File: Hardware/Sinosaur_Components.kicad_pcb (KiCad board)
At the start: 4 copper layers, 60 x 100 mm, 82 parts, among them J1 Conn_01x12_Male, J2 Conn_01x12_Male, J3 Conn_01x16_Male, J4 Conn_01x16_Male, J5 SWD_Header, J6 Eurorack_16_pin_power, J7 UART_Test_Pins, J8 USB_B_Micro, Q1 MMBT3904, Q2 MMBT3904, U1 STM32G473V, U2 STF202-22T1G, U3 TL074, U4 TL074, U5 LT1117-3.3, Y1 8MHz 20pF

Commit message: Updated file names
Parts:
- moved TP3 55.7 mm to (114.8, 62.2)
- moved TP1 29.1 mm to (143.3, 68.6)
- moved C9 0.50 mm to (117.0, 106.0)
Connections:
- J1 pad 10: unconnected-(J1-Pin_10-Pad10) -> GND
- J2 pad 3: +3.3V -> unconnected-(J2-Pin_3-Pad3)
- J3 pad 12: unconnected-(J3-Pin_12-Pad12) -> /Sine2_Rate
- J3 pad 13: unconnected-(J3-Pin_13-Pad13) -> GND
- J3 pad 14: unconnected-(J3-Pin_14-Pad14) -> +3.3V
- J3 pad 6: /Sine3_Ramp_Lvl_LED -> GND
- J3 pad 7: /Sine1_Swell_Lvl_LED -> /Sine3_Ramp_Lvl_LED
- J3 pad 8: /Sine2_Swell_Lvl_LED -> /Sine1_Swell_Lvl_LED
- J3 pad 9: unconnected-(J3-Pin_9-Pad9) -> /Sine2_Swell_Lvl_LED
- J4 pad 10: /Sine1_Rate_Btn -> /Sine2_Rate_Btn
- J4 pad 11: /Sine3_Lvl_Btn -> /Sine1_Rate_Btn
- J4 pad 12: /Sine2_Lvl_Btn -> /Sine3_Lvl_Btn
- J4 pad 13: /Sine1_Lvl_Btn -> /Sine2_Lvl_Btn
- J4 pad 14: /Gate_In -> /Sine1_Lvl_Btn
- J4 pad 15: /Clock_In -> /Gate_In
- J4 pad 16: GND -> /Clock_In
- J4 pad 8: /Sine3_Rate_Btn -> GND
- J4 pad 9: /Sine2_Rate_Btn -> /Sine3_Rate_Btn
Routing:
- net +3.3V: track 35.6 -> 199.4 mm, vias 0 -> 8
- net /Sine2_Rate: track 0.00 -> 48.6 mm, vias 0 -> 1
- net +3.3VA: track 17.4 -> 53.9 mm, vias 2 -> 3
- net -12V: track 66.6 -> 92.6 mm
- net /Swell_DAC: track 34.5 -> 41.2 mm
- net /Gate_Scaled: track 41.5 -> 44.1 mm
- net /Sine1_Swell_Lvl_LED: track 15.6 -> 18.2 mm
- net /Sine2_Swell_Lvl_LED: track 16.6 -> 19.1 mm
- net /Sine3_Ramp_Lvl_LED: track 14.9 -> 17.4 mm
- net /Sine1_Rate: track 44.6 -> 46.5 mm
- net +12V: track 59.6 -> 61.5 mm
- net /TIM2_CH2: track 24.1 -> 25.3 mm
- net /Sine2_Rate_Btn: track 42.0 -> 43.1 mm
- net /Sine1_Lvl_Btn: track 49.4 -> 50.5 mm
- net /Sine3_Rate_Btn: track 40.2 -> 41.2 mm
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
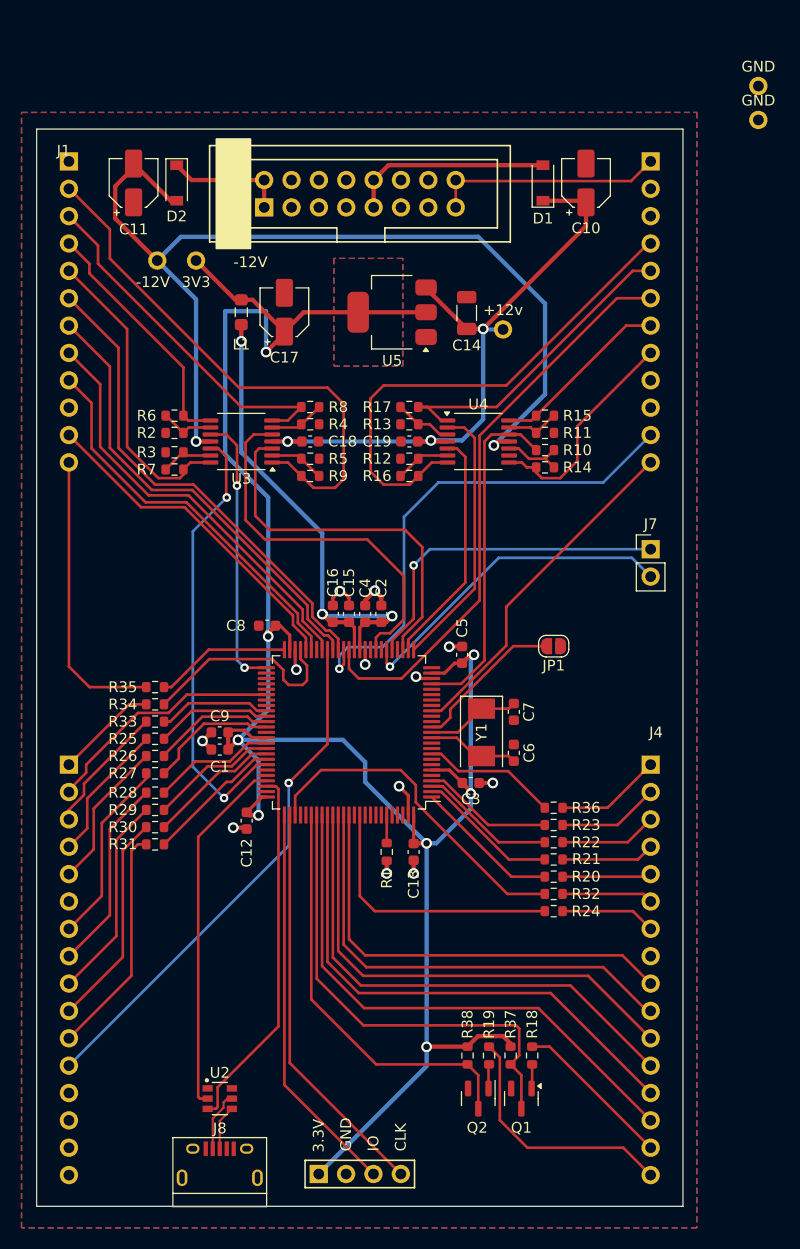
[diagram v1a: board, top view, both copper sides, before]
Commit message: Control PCB wiring
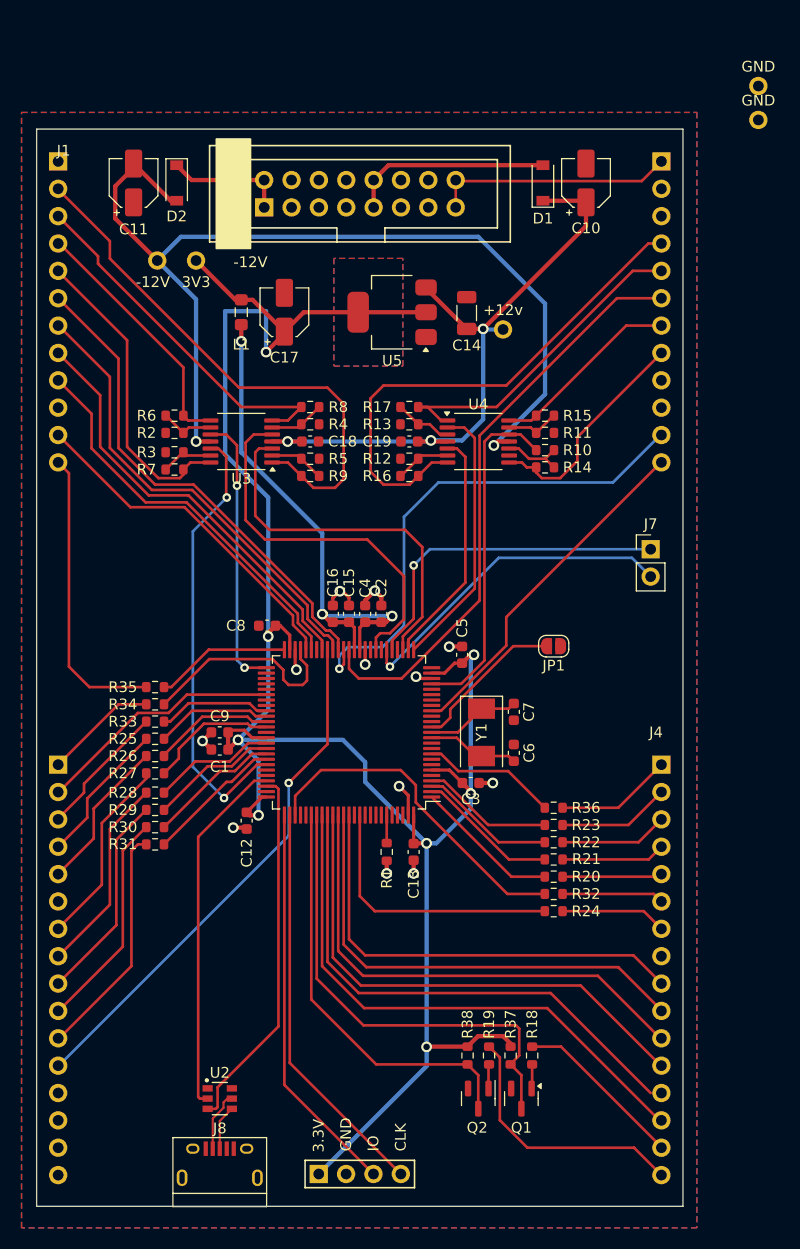
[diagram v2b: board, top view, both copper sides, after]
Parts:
- R25, R26, R27, R28, R29, R30, R31, R32, R33, R34, R35, R36: value 560 -> 1k
- moved J1 1.00 mm to (102.0, 53.0)
- moved J2 1.00 mm to (158.0, 53.0)
- moved J3 1.00 mm to (102.0, 109.0)
- moved J4 1.00 mm to (158.0, 109.0)
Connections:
- J1 pad 8: /Sine3_Rate -> /Swell_Level
- J2 pad 12: /Swell_Level -> /Sine3_Rate
- J2 pad 3: unconnected-(J2-Pin_3-Pad3) -> GND
- J3 pad 15: unconnected-(J3-Pin_15-Pad15) -> GND
- U1 pad 17: /Swell_Level -> /Sine3_Rate
- U1 pad 43: /Sine3_Rate -> /Swell_Level
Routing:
- net /Swell_Level: track 32.0 -> 39.9 mm
- net /Sine3_Rate: track 39.4 -> 32.4 mm
- net /Sine2_Rate_Btn: track 43.1 -> 44.1 mm
- net /Gate_In: track 14.9 -> 15.9 mm
- net /Sine3_Rate_Btn: track 41.2 -> 42.2 mm
- net /Sine3_Level: track 53.7 -> 54.7 mm
- net /Sine1_Rate_Btn: track 45.0 -> 46.0 mm
- net /Swell_LED: track 8.66 -> 9.66 mm
- net /Sine3_Swell_Rate_LED: track 9.83 -> 10.8 mm
- net /Sine3_Out: track 30.0 -> 31.0 mm
- net /Sine3_Lvl_Btn: track 46.9 -> 47.9 mm
- net /Sine3_LED: track 8.85 -> 9.85 mm
- net /Sine2_Ramp_Rate_LED: track 8.46 -> 9.46 mm
- net /Sine2_Out: track 47.2 -> 48.2 mm
- net /Sine2_LED: track 9.44 -> 10.4 mm
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
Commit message: Updates to LEDs
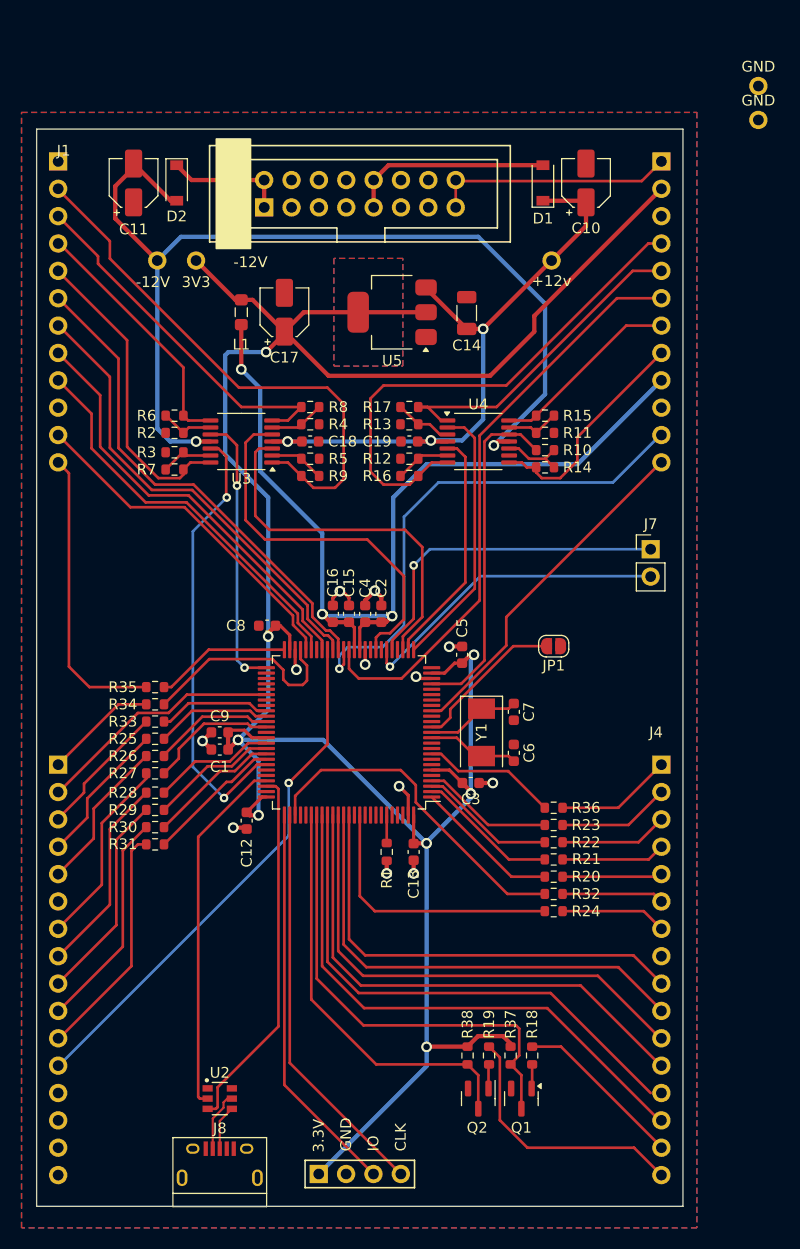
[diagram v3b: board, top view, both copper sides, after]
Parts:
- moved TP1 7.82 mm to (147.8, 62.2)
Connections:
- J2 pad 2: GND -> +3.3V
- J3 pad 14: +3.3V -> GND
- J3 pad 16: unconnected-(J3-Pin_16-Pad16) -> GND
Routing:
- net +3.3VA: track 53.9 -> 94.4 mm
- net +3.3V: track 199.4 -> 234.8 mm
- net +12V: track 61.5 -> 59.7 mm
- net /USART1_RX: track 30.8 -> 29.4 mm
- net -12V: track 92.6 -> 94.0 mm

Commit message: Gerber production
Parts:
- added TP6: TestPoint, Custom_Footprints:1mm_Test_Point, F.Cu at (106.1, 93.8)
- U3, U4: footprint Package_SO:TSSOP-14_4.4x5mm_P0.65mm -> Package_SO:SOIC-14_3.9x8.7mm_P1.27mm
- moved TP5 100.3 mm to (143.0, 146.5)
- moved TP4 54.5 mm to (157.0, 99.6)
- moved TP3 35.6 mm to (150.4, 62.1)
- moved TP1 1.20 mm to (146.6, 62.1)
- moved R10 0.80 mm to (147.2, 80.6), turned to 0 degrees
- moved R11 0.80 mm to (147.2, 77.4)
- moved R14 0.80 mm to (147.2, 82.2), turned to 180 degrees
- moved R15 0.80 mm to (147.2, 75.8)
- moved R2 0.80 mm to (112.8, 77.4)
- moved R6 0.80 mm to (112.8, 75.8)
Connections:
- R10 pad 1: Net-(U4C-+) -> Net-(U4C--)
- R13 pad 2: Net-(U4A-+) -> Net-(U4A--)
- R14 pad 2: Net-(U4C-+) -> Net-(U4C--)
- R17 pad 2: Net-(U4A-+) -> Net-(U4A--)
- U1 pad 10: unconnected-(U1-PF9-Pad10) -> /Sine3_Swell_Rate
- U1 pad 9: /Sine3_Swell_Rate -> unconnected-(U1-PC15-Pad9)
- U4 pad 10: Net-(U4C-+) -> GND
- U4 pad 2: /Sine3_DAC -> Net-(U4A--)
- U4 pad 3: Net-(U4A-+) -> /Sine3_DAC
- U4 pad 9: GND -> Net-(U4C--)
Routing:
- net GND: track 23.3 -> 36.3 mm, vias 12 -> 75
- net +3.3V: track 234.8 -> 228.1 mm, vias 8 -> 30
- net Net-(U4C-+): track 6.02 -> 0.00 mm
- net Net-(U4A--): track 0.00 -> 5.80 mm
- net Net-(U4A-+): track 5.42 -> 0.00 mm
- net Net-(U4C--): track 0.00 -> 4.51 mm
- net +12V: track 59.7 -> 63.9 mm
- net /Sine1_DAC: track 31.8 -> 35.6 mm
- net -12V: track 94.0 -> 90.4 mm
- net /FM2_Out: track 33.6 -> 30.3 mm
- net /Sine3_Out: track 31.0 -> 27.8 mm
- net /Swell_DAC: track 41.2 -> 38.3 mm
- net /Sine3_Level: track 54.7 -> 56.2 mm
- net /Sine2_Lvl_Btn: track 48.7 -> 49.6 mm
- net Net-(U3D--): track 4.95 -> 5.85 mm
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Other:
- board text added: "J2"
- board text added: "J3"
- board text added: "Mountjoy Modular 2024 Sinosaur Components v1.0"
- board text added: "RX"
- board text added: "Reset"
- board text added: "TX"

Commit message: Gerber production for v1
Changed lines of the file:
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@@
-	)
-	(segment
-		(start 122.3 79)
-		(end 121.475 79)
-		(width 0.4)
-		(layer "F.Cu")
-		(net 5)
 	)
 	(segment
 		(start 147 56.65)
 		(end 150.85 56.65)
-		(width 0.4)
-		(layer "F.Cu")
-		(net 5)
-	)
-	(segment
-		(start 121.8625 79)
-		(end 124.625 79)
 		(width 0.4)
 		(layer "F.Cu")
@@
 	)
 	(segment
+		(start 123.3 80)
+		(end 123.625 80)
+		(width 0.4)
+		(layer "F.Cu")
+		(net 5)
+	)
+	(segment
 		(start 151 57.7)
 		(end 141.45 67.25)
@@
 		(start 136.175 79.8)
 		(end 135.375 79)
-		(width 0.4)
-		(layer "F.Cu")
-		(net 5)
-	)
-	(segment
-		(start 123.3 80)
-		(end 122.3 79)
 		(width 0.4)
 		(layer "F.Cu")
@@
 	)
 	(segment
+		(start 123.625 80)
+		(end 124.625 79)
+		(width 0.4)
+		(layer "F.Cu")
+		(net 5)
+	)
+	(segment
 		(start 141.45 68.55)
 		(end 139.925 68.55)
 		(width 0.4)
 		(layer "F.Cu")
+		(net 5)
+	)
+	(segment
+		(start 124.625 79)
+		(end 121.475 79)
+		(width 0.4)
+		(layer "F.Cu")
